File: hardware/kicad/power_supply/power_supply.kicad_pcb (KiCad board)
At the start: 2 copper layers, 57 x 24 mm, 36 parts, among them J1 USB_C_Receptacle_PowerOnly_6P, J2 PINHD_1x4_Female, M1 MountingHole_2.7mm, M2 MountingHole_2.7mm, M3 MountingHole_2.2mm_M2, M4 MountingHole_2.2mm_M2, M5 MountingHole_2.2mm_M2, M6 MountingHole_2.7mm, Q1 AO3401A, U1 TP4056-42-ESOP8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

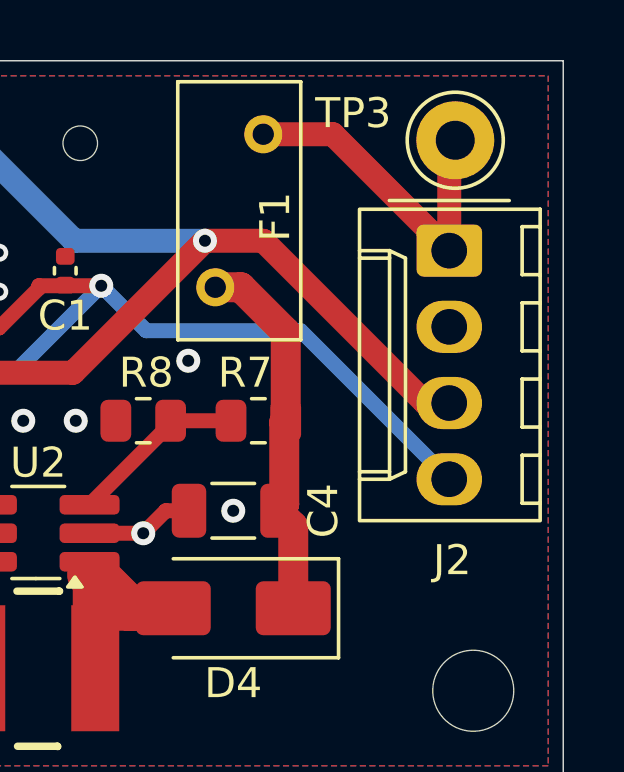
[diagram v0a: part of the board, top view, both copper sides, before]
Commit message: Visual changes on KiCAD projects
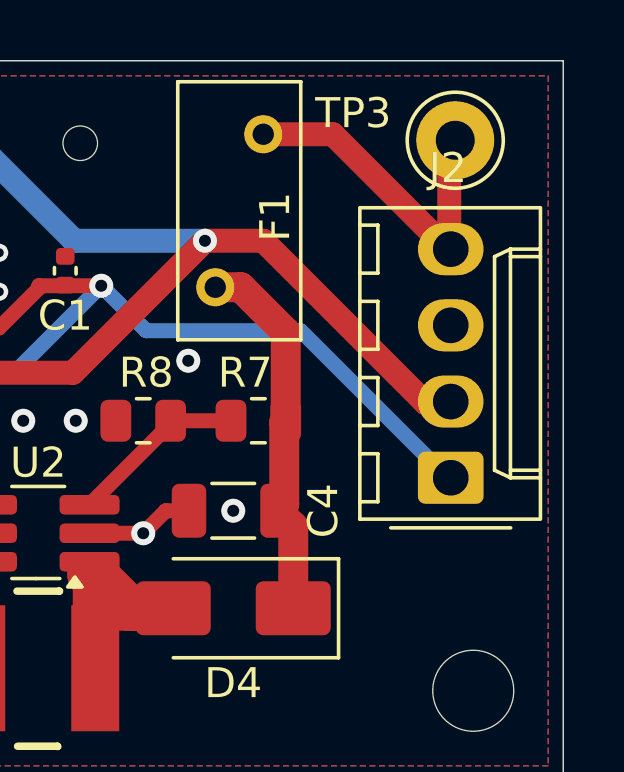
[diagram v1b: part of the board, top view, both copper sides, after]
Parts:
- moved J2 7.57 mm to (169.6, 96.1), turned to 90 degrees
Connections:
- net Net-(D4-K) renamed /Boost_{OUT}
- J2 pad 1: Net-(J2-Vout) -> V_{bat}
- J2 pad 2: GND -> V_{in}
- J2 pad 3: V_{in} -> GND
- J2 pad 4: V_{bat} -> Net-(J2-Vout)
